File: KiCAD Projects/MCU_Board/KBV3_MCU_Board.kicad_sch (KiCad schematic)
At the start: 3 parts, among them J1 Conn_01x06, J2 USB_C_Receptacle, U1 ATSAMD21J18A-A

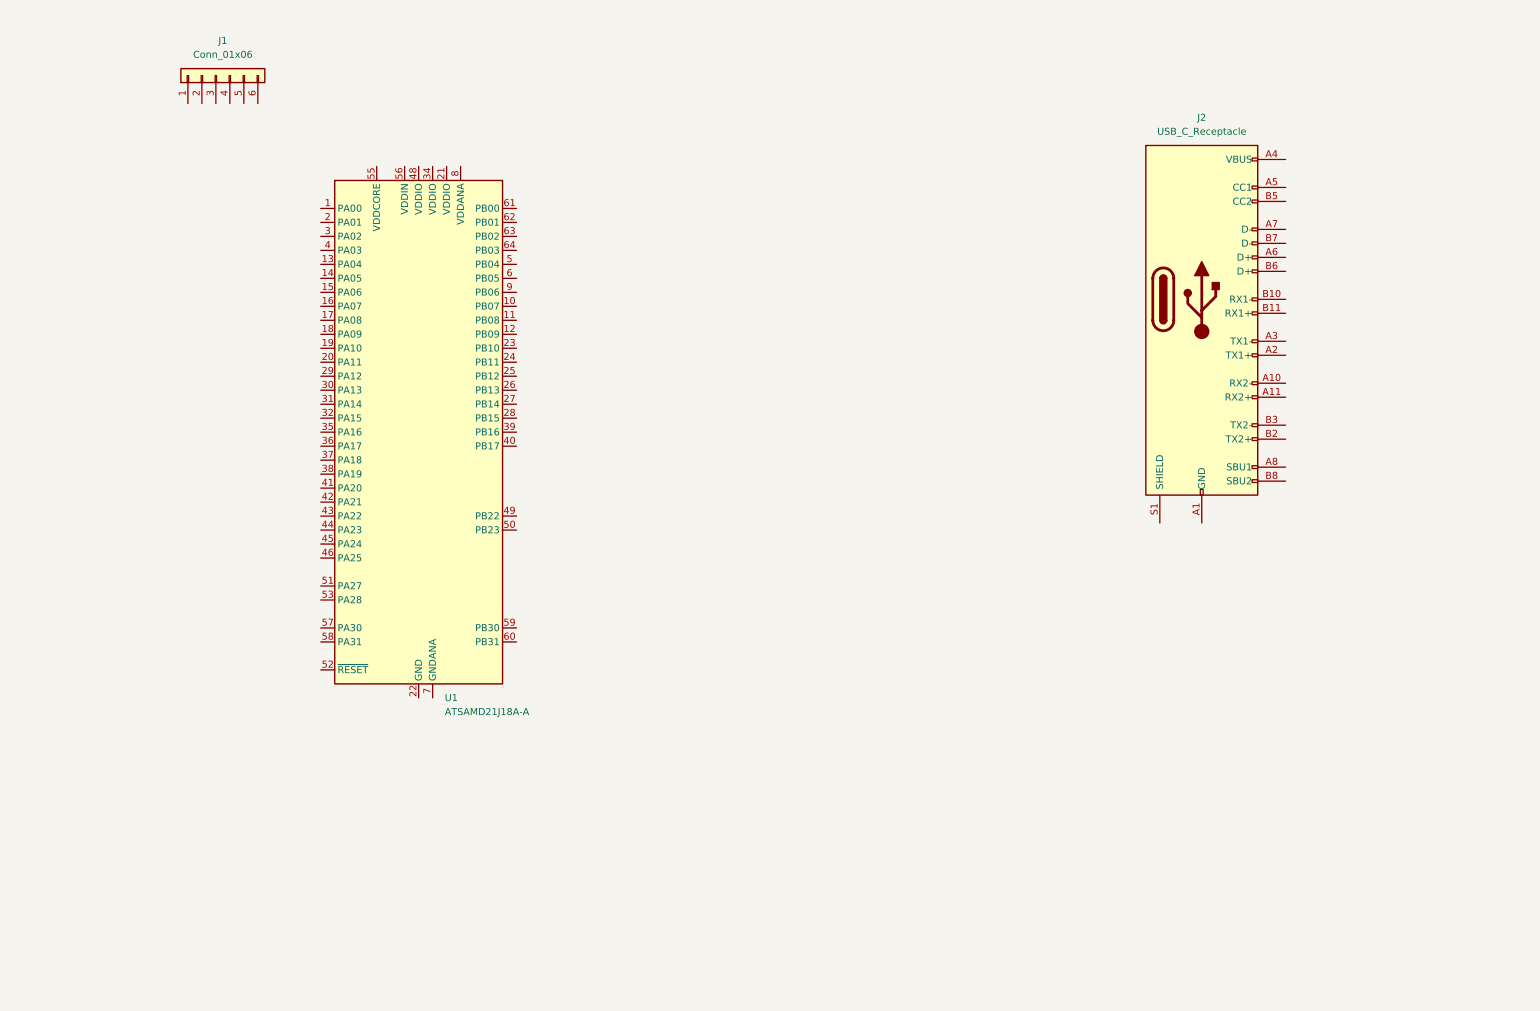
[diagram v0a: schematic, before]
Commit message: Clean Libraries, Added Datasheet, LDO, etc
Cleaned up some of the footprints that are not needed. Added components for PD and voltage regulation. Only minor changes to schematic
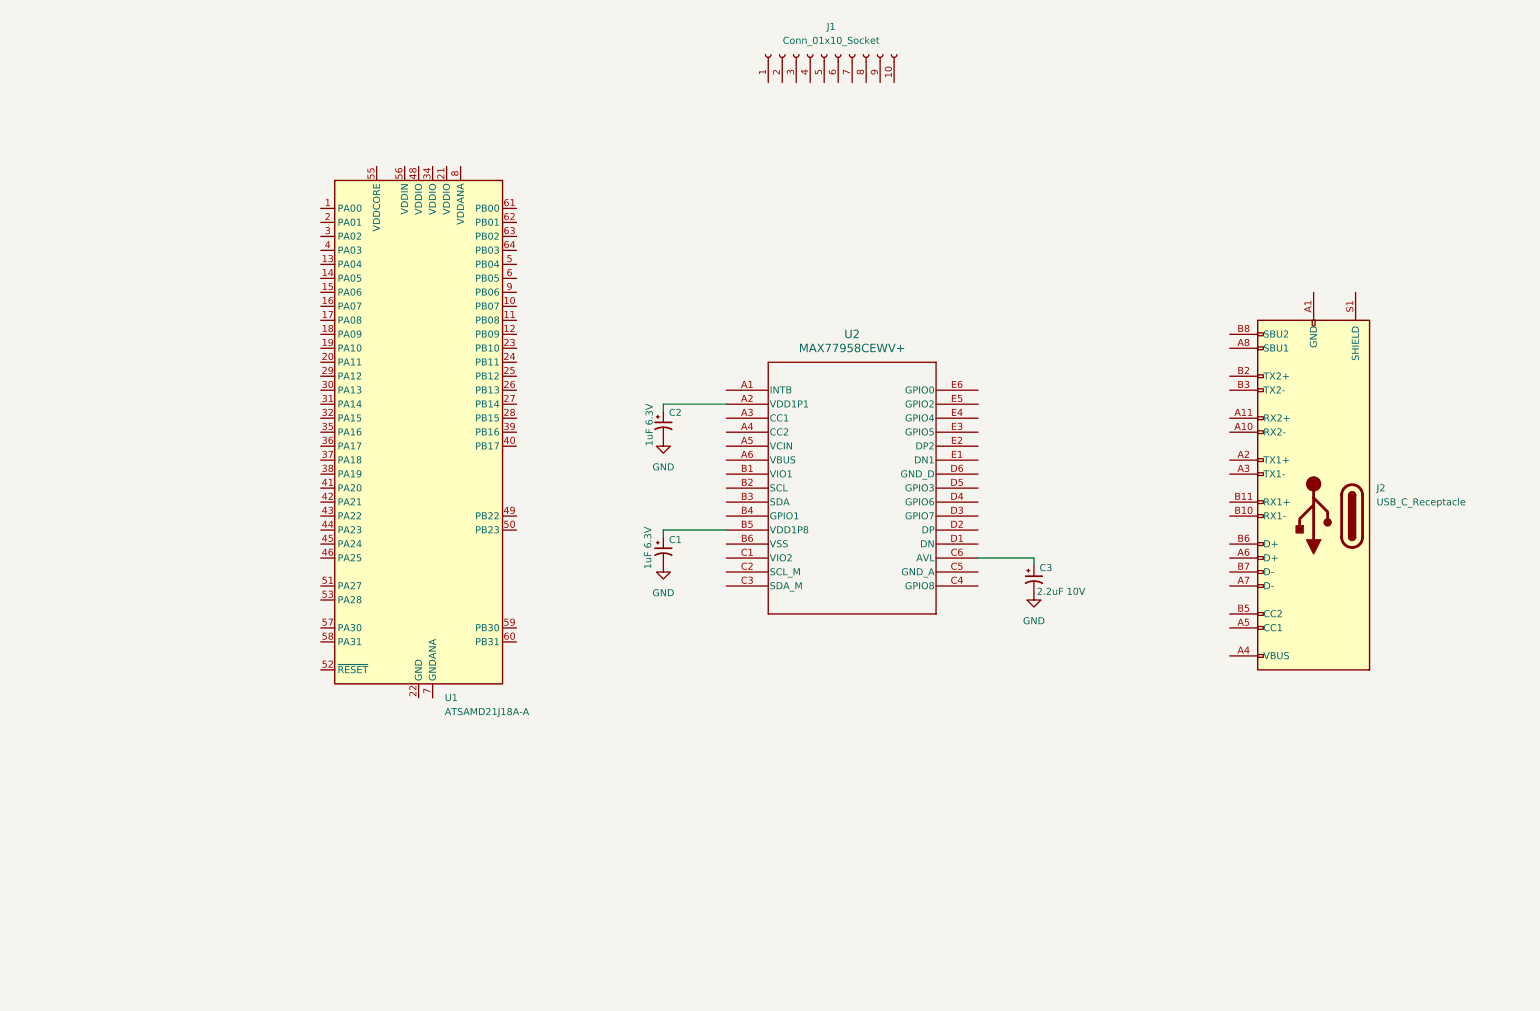
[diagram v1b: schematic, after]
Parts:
- removed J1: Conn_01x06, symbol Connector_Generic:Conn_01x06
- added C1, C2: 1uF 6.3V, symbol Device:C_Polarized_Small_US
- added C3: 2.2uF 10V, symbol Device:C_Polarized_Small_US
- added J1: Conn_01x10_Socket, symbol Connector:Conn_01x10_Socket
- added U2: MAX77958CEWV+, 21-100339_W302B3+1_ADI, symbol MAX77958:MAX77958CEWV+
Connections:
- new net: C2.1, U2.A2 (VDD1P1)
- new net: C1.1, U2.B5 (VDD1P8)
- new net: C3.1, U2.C6 (AVL)
- new net GND: C1.2, C2.2, C3.2
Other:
- moved on the sheet: J2

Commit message: schematic changes to MCU board and added some quick reference screenshots
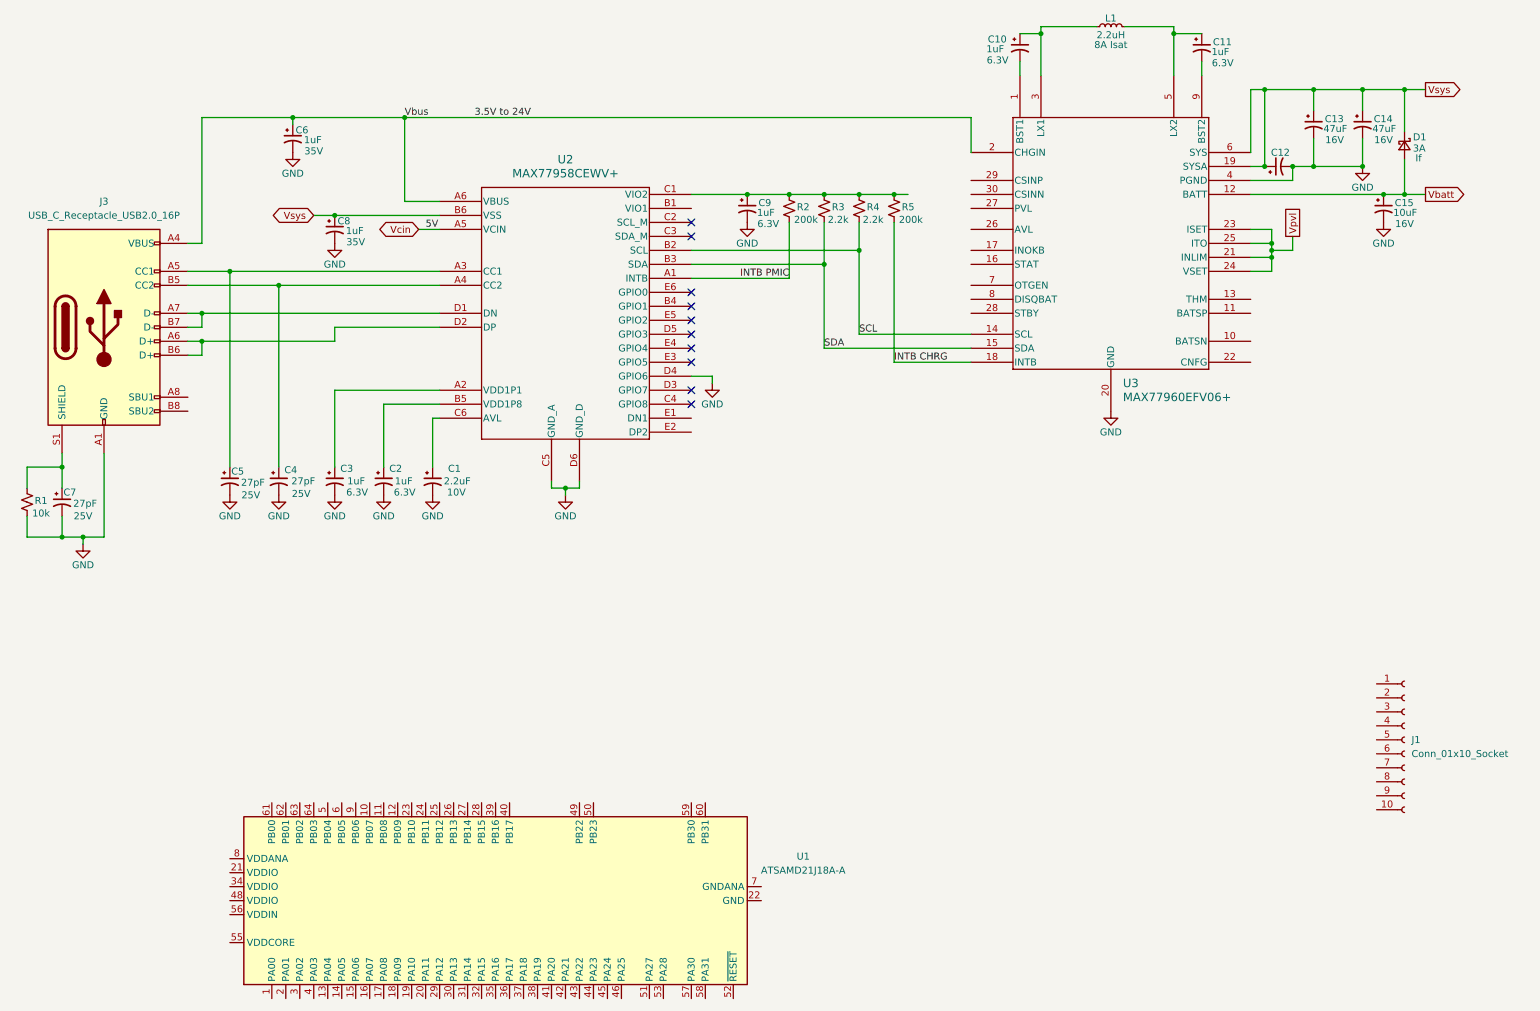
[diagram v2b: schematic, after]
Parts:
- removed C1: 1uF 6.3V, symbol Device:C_Polarized_Small_US
- removed J2: USB_C_Receptacle, symbol Connector:USB_C_Receptacle
- removed U2: MAX77958CEWV+, 21-100339_W302B3+1_ADI, symbol MAX77958:MAX77958CEWV+
- added C10, C11, C2, C6, C8, C9: 1uF, symbol Device:C_Polarized_Small_US
- added C12: ~, symbol Device:C_Polarized_Small_US
- added C13, C14: 47uF, symbol Device:C_Polarized_Small_US
- added C15: 10uF, symbol Device:C_Polarized_Small_US
- added C4, C5, C7: 27pF, symbol Device:C_Polarized_Small_US
- added D1: 3A, symbol Device:D_Schottky_Small
- added J3: USB_C_Receptacle_USB2.0_16P, symbol Connector:USB_C_Receptacle_USB2.0_16P
- added L1: 2.2uH, symbol Device:L_Small
- added R1: 10k, symbol Device:R_Small_US
- added R2, R5: 200k, symbol Device:R_Small_US
- added R3, R4: 2.2k, symbol Device:R_Small_US
- added U2: MAX77958CEWV+, 21-100339_W302B3+1_ADI, symbol USBPD_CHIP_MAX77958:MAX77958CEWV+
- added U3: MAX77960EFV06+, 21-100278_90-100100A_MXM, symbol Battery_Charger_MAX77960EFV06+:MAX77960EFV06+
- C1: renamed from C3; value 2.2uF 10V -> 2.2uF; Field5 (none) -> 10V
- C3: renamed from C2; value 1uF 6.3V -> 1uF; Field5 (none) -> 6.3V
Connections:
- net GND: now also C12.2, C13.2, C14.2, C15.2, C2.2, C4.2, C5.2, C6.2, C7.2, C8.2, C9.2, J3.A1 (GND), J3.A12 (GND), J3.B1 (GND), J3.B12 (GND), R1.1, U2.C5 (GND_A), U2.D4 (GPIO6), U2.D6 (GND_D), U3.20 (GND), U3.4 (PGND)
- net at C3.1: now also U2.A2 (VDD1P1)
- net at C1.1: now also U2.C6 (AVL)
- new net: C11.1, L1.2, U3.5 (LX2)
- new net: C11.2, U3.9 (BST2)
- new net: C4.1, J3.B5 (CC2), U2.A4 (CC2)
- new net: C10.2, U3.1 (BST1)
- new net: C10.1, L1.1, U3.3 (LX1)
- new net: C7.1, J3.S1 (SHIELD), R1.2
- new net: C9.1, R2.2, R3.2, R4.2, R5.2, U2.C1 (VIO2)
- new net: C5.1, J3.A5 (CC1), U2.A3 (CC1)
- new net: J3.A6 (D+), J3.B6 (D+), U2.D2 (DP)
- new net: J3.A7 (D-), J3.B7 (D-), U2.D1 (DN)
- new net: C2.1, U2.B5 (VDD1P8)
- new net 3.5V to 24V: C6.1, J3.A4 (VBUS), J3.A9 (VBUS), J3.B4 (VBUS), J3.B9 (VBUS), U2.A6 (VBUS), U3.2 (CHGIN)
- new net INTB CHRG: R5.1, U3.18 (INTB)
- new net INTB PMIC: R2.1, U2.A1 (INTB)
- new net SCL: R4.1, U2.B2 (SCL), U3.14 (SCL)
- new net SDA: R3.1, U2.B3 (SDA), U3.15 (SDA)
- new net Vbatt: C15.1, D1.2 (A), U3.12 (BATT)
- new net Vcin: U2.A5 (VCIN)
- new net Vpvl: U3.21 (INLIM), U3.23 (ISET), U3.24 (VSET), U3.25 (ITO)
- new net Vsys: C12.1, C13.1, C14.1, C8.1, D1.1 (K), U2.B6 (VSS), U3.19 (SYSA), U3.6 (SYS)
- no-connect marks 0 -> 10
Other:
- moved on the sheet: C1, C3, J1, U1

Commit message: Changed the key matrix to one row 6 instead of two smaller rows.  Added USB ESD protection
Changed the key matrix to one row 6 instead of two smaller rows.

Added USB ESD protection
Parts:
- added CR1: USBLC6-2SC6, SOT23-6L_STM, symbol USB_ESD_USBLC6-2SC6:USBLC6-2SC6
- added U4: ATtiny85-20S, Package_SO:SOIC-8W_5.3x5.3mm_P1.27mm, symbol MCU_Microchip_ATtiny:ATtiny85-20S
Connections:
- net GND: now also CR1.1, CR1.2, CR1.3
- net D+: now reaches J3.A6 (D+), J3.B6 (D+), U2.D2 (DP)
- net D+: now also CR1.6
- net at J3.A7 (D-), U2.D1 (DN): no longer J3.B7 (D-)
- net 3.5V to 24V renamed Vbus
- net Vbus: now also CR1.5
- new net D-: CR1.4, J3.B7 (D-)
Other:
- note added: "To USBLC6"
- moved on the sheet: C1, C2, C3, C4, C5, C6, C7, R1, U1, U2
